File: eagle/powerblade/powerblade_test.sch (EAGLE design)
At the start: 139 parts, among them J1 JTAG_14PIN_IDC, J21 AC_INSW, Q1 2SK1829, Q2 2SK1829, Q3 2SK1829, U1 TPS62122, U2 TR1000, U3 MSP430FR5738, U4 LTC5800, U5 MAX9910, U6 MAX9910, U7 OPA2369, X1 ABM8G, X2 ABS07, X3 32.768kHz, Y1 UREACH_XTEND, Y2 ANT-916

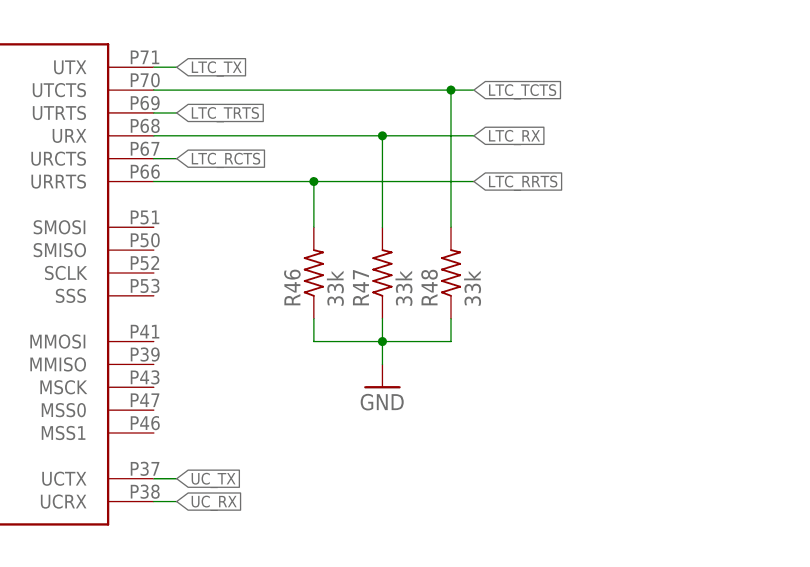
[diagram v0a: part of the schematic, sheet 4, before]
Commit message: finished doing parts for powerblade test
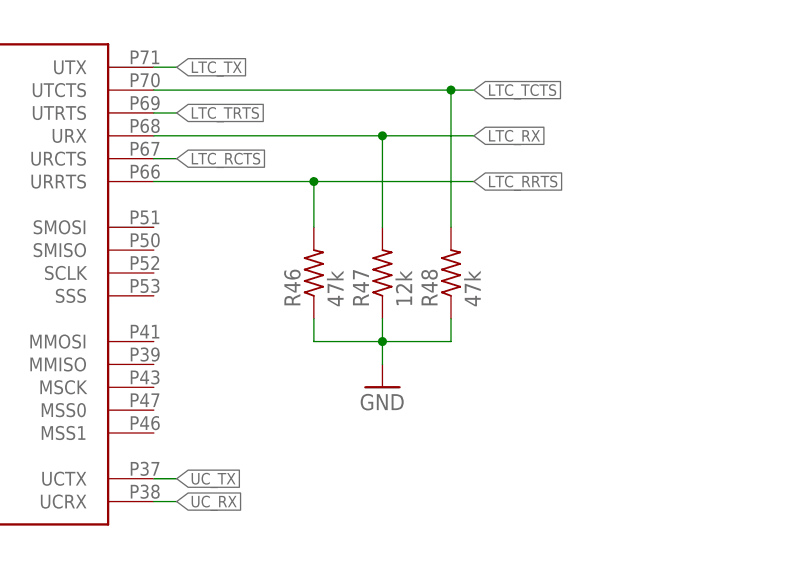
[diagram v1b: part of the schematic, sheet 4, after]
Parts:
- ACSLOT, C30, D2, D3, J21, R33, R34, TP10, TP11, TP12, TP13, TP14, TP2, TP5, TP6, TP7: DIGIKEY (none) -> NP
- C1: DIGIKEY 490-4238-1-ND -> 490-5919-1-ND
- C11, C12, C13, C17, C18, C19, C20, C21, C5, C6: DIGIKEY (none) -> 490-6324-1-ND
- C22, C25: DIGIKEY (none) -> 445-1316-1-ND
- C23: DIGIKEY (none) -> 1276-2377-1-ND
- C24: DIGIKEY (none) -> 445-1318-1-ND
- C26: DIGIKEY (none) -> 1276-2368-1-ND
- C29: DIGIKEY (none) -> 490-6209-1-ND
- C31, R16, R43: DIGIKEY (none) -> P0.0JCT-ND
- C33: DIGIKEY (none) -> 445-5091-1-ND
- C35: DIGIKEY (none) -> 445-1274-1-ND
- C36: DIGIKEY (none) -> 445-1281-1-ND
- C37: DIGIKEY (none) -> 478-8120-1-ND
- C39: DIGIKEY (none) -> 445-13874-1-ND
- C4: DIGIKEY (none) -> 1276-1116-1-ND
- C7: DIGIKEY 490-5915-1-ND -> 1276-1784-1-ND
- CS+: DIGIKEY NP -> 5012K-ND
- CS-: DIGIKEY NP -> 5010K-ND
- D1: DIGIKEY BZT52C10T-7DICT-ND -> NP; DIGIKEY_2 BZT52C15T-7DICT-ND -> (none)
- HVS: DIGIKEY 5000K-ND -> 5013K-ND
- L2: DIGIKEY (none) -> 490-4023-1-ND
- L3: DIGIKEY (none) -> 732-3452-1-ND
- L4: DIGIKEY (none) -> 490-6760-1-ND
- L5: DIGIKEY (none) -> 732-2924-1-ND
- L6: DIGIKEY (none) -> CW100505-R10JCT-ND
- R10, R23: DIGIKEY (none) -> P120GCT-ND
- R11: DIGIKEY (none) -> P133KHCT-ND
- R12: DIGIKEY (none) -> P66.5KHCT-ND
- R13: DIGIKEY CRT0603-BY-10R0ELFCT-ND -> P1.0AJCT-ND
- R14: DIGIKEY (none) -> P200LCT-ND
- R17: DIGIKEY (none) -> P20.0KLCT-ND
- R18: DIGIKEY (none) -> 541-2.49LLCT-ND
- R20, R21: DIGIKEY (none) -> P10.0KLCT-ND
- R22: DIGIKEY (none) -> P270KGCT-ND
- R26, R29: DIGIKEY (none) -> P100KGCT-ND
- R28: DIGIKEY (none) -> P330KGCT-ND
- R30: DIGIKEY (none) -> P4.7KGCT-ND
- R31, R32: value 4.99k -> 47k; DIGIKEY (none) -> P47KGCT-ND
- R35: DIGIKEY (none) -> P2.00KLCT-ND
- R37: DIGIKEY (none) -> P90.9KLCT-ND
- R38: DIGIKEY (none) -> P3.09KHCT-ND
- R40: DIGIKEY (none) -> P100KLCT-ND
- R44: DIGIKEY (none) -> P47KJCT-ND
- R45: DIGIKEY (none) -> P12KJCT-ND
- R46, R48: value 33k -> 47k; DIGIKEY (none) -> P47KJCT-ND
- R47: value 33k -> 12k; DIGIKEY (none) -> P12KJCT-ND
- R49: DIGIKEY (none) -> P47KGCT-ND
- R7: DIGIKEY (none) -> P560KLCT-ND
- R9: DIGIKEY (none) -> P180KLCT-ND
- RF: DIGIKEY (none) -> P1.50KLCT-ND
- RI1, RI2: DIGIKEY (none) -> P220KLCT-ND
- RS+: DIGIKEY NP -> 5014K-ND
- TP1, TP4, TP9: DIGIKEY (none) -> 5126K-ND
- TP3: DIGIKEY (none) -> 5129K-ND
- TPGND1, TPGND2: DIGIKEY NP -> 5011K-ND
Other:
- note added: "Black"
- note added: "Orange"
